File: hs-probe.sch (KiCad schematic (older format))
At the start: 55 parts, among them J1 USB_C_Receptacle_USB2.0, J2 Castellated Vias, J3 Castellated Vias, J4 Castellated Vias, J5 tag-connect-swd, U1 base-stm32, U2 12 MHz, U3 MIC5353, U4 NUF8401MNT4G, U5 STDC14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

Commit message: Revert accidential commits that should have gone to a fork
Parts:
- U1: value base-stm32 -> hs-probe-stm32; symbol base-stm32:base-stm32 -> hs-probe-stm32:hs-probe-stm32
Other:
- note added: "Designed by: Emil Fresk\nTwitter / Github: @korken89\nLink: https://github.com/probe-rs/hs-probe"
- note removed: "Designed by: Emil Fresk\nTwitter / Github: @korken89\nLink: https://github.com/probe-rs/base"
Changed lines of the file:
@@
 MCU I/O
 $Comp
-L base-stm32:base-stm32 U1
+L hs-probe-stm32:hs-probe-stm32 U1
 U 9 1 5F18CA2E
 P 5550 5500
 F 0 "U1" H 6042 5787 60  0000 C CNN
-F 1 "base-stm32" H 6042 5681 60  0000 C CNN
+F 1 "hs-probe-stm32" H 6042 5681 60  0000 C CNN
 F 2 "bga:UFBGA-201_10x10mm_Layout15x15_P0.65mm" H 5750 5550 60  0001 L CNN
 F 3 "" H 5750 5350 60  0001 L CNN
@@
 $EndComp
 $Comp
-L base-stm32:base-stm32 U1
+L hs-probe-stm32:hs-probe-stm32 U1
 U 7 1 5F17D932
 P 3900 9500
 F 0 "U1" H 4342 9787 60  0000 C CNN
-F 1 "base-stm32" H 4342 9681 60  0000 C CNN
+F 1 "hs-probe-stm32" H 4342 9681 60  0000 C CNN
 F 2 "bga:UFBGA-201_10x10mm_Layout15x15_P0.65mm" H 4100 9550 60  0001 L CNN
 F 3 "" H 4100 9350 60  0001 L CNN
@@
 $EndComp
 $Comp
-L base-stm32:base-stm32 U1
+L hs-probe-stm32:hs-probe-stm32 U1
 U 5 1 5F175F3E
 P 3900 7500
 F 0 "U1" H 4342 7787 60  0000 C CNN
-F 1 "base-stm32" H 4342 7681 60  0000 C CNN
+F 1 "hs-probe-stm32" H 4342 7681 60  0000 C CNN
 F 2 "bga:UFBGA-201_10x10mm_Layout15x15_P0.65mm" H 4100 7550 60  0001 L CNN
 F 3 "" H 4100 7350 60  0001 L CNN
@@
 $EndComp
 $Comp
-L base-stm32:base-stm32 U1
+L hs-probe-stm32:hs-probe-stm32 U1
 U 4 1 5F17144F
 P 3900 5500
 F 0 "U1" H 4392 5787 60  0000 C CNN
-F 1 "base-stm32" H 4392 5681 60  0000 C CNN
+F 1 "hs-probe-stm32" H 4392 5681 60  0000 C CNN
 F 2 "bga:UFBGA-201_10x10mm_Layout15x15_P0.65mm" H 4100 5550 60  0001 L CNN
 F 3 "" H 4100 5350 60  0001 L CNN
@@
 $EndComp
 $Comp
-L base-stm32:base-stm32 U1
+L hs-probe-stm32:hs-probe-stm32 U1
 U 3 1 5F16E354
 P 2150 9300
 F 0 "U1" H 2642 9587 60  0000 C CNN
-F 1 "base-stm32" H 2642 9481 60  0000 C CNN
+F 1 "hs-probe-stm32" H 2642 9481 60  0000 C CNN
 F 2 "bga:UFBGA-201_10x10mm_Layout15x15_P0.65mm" H 2350 9350 60  0001 L CNN
 F 3 "" H 2350 9150 60  0001 L CNN
@@
 $EndComp
 $Comp
-L base-stm32:base-stm32 U1
+L hs-probe-stm32:hs-probe-stm32 U1
 U 2 1 5F165849
 P 2150 7300
 F 0 "U1" H 2792 7587 60  0000 C CNN
-F 1 "base-stm32" H 2792 7481 60  0000 C CNN
+F 1 "hs-probe-stm32" H 2792 7481 60  0000 C CNN
 F 2 "bga:UFBGA-201_10x10mm_Layout15x15_P0.65mm" H 2350 7350 60  0001 L CNN
 F 3 "" H 2350 7150 60  0001 L CNN
@@
 $EndComp
 $Comp
-L base-stm32:base-stm32 U1
+L hs-probe-stm32:hs-probe-stm32 U1
 U 1 1 5F160B70
 P 2150 5500
 F 0 "U1" H 2792 5787 60  0000 C CNN
-F 1 "base-stm32" H 2792 5681 60  0000 C CNN
+F 1 "hs-probe-stm32" H 2792 5681 60  0000 C CNN
 F 2 "bga:UFBGA-201_10x10mm_Layout15x15_P0.65mm" H 2350 5550 60  0001 L CNN
 F 3 "" H 2350 5350 60  0001 L CNN
@@
 $EndComp
 $Comp
-L base-stm32:base-stm32 U1
+L hs-probe-stm32:hs-probe-stm32 U1
 U 12 1 5F19B372
 P 1550 2000
 F 0 "U1" H 1892 2287 60  0000 C CNN
-F 1 "base-stm32" H 1892 2181 60  0000 C CNN
+F 1 "hs-probe-stm32" H 1892 2181 60  0000 C CNN
 F 2 "bga:UFBGA-201_10x10mm_Layout15x15_P0.65mm" H 1750 2050 60  0001 L CNN
 F 3 "" H 1750 1850 60  0001 L CNN
@@
 $EndComp
 $Comp
-L base-stm32:base-stm32 U1
+L hs-probe-stm32:hs-probe-stm32 U1
 U 11 1 5F19563C
 P 4100 2000
 F 0 "U1" H 4517 2287 60  0000 C CNN
-F 1 "base-stm32" H 4517 2181 60  0000 C CNN
+F 1 "hs-probe-stm32" H 4517 2181 60  0000 C CNN
 F 2 "bga:UFBGA-201_10x10mm_Layout15x15_P0.65mm" H 4300 2050 60  0001 L CNN
 F 3 "" H 4300 1850 60  0001 L CNN
@@
 $EndComp
 $Comp
-L base-stm32:base-stm32 U1
+L hs-probe-stm32:hs-probe-stm32 U1
 U 10 1 5F190F67
 P 2350 3650
 F 0 "U1" H 3092 3937 60  0000 C CNN
-F 1 "base-stm32" H 3092 3831 60  0000 C CNN
+F 1 "hs-probe-stm32" H 3092 3831 60  0000 C CNN
 F 2 "bga:UFBGA-201_10x10mm_Layout15x15_P0.65mm" H 2550 3700 60  0001 L CNN
 F 3 "" H 2550 3500 60  0001 L CNN
@@
 SPI1_MOSI
 Text Notes 11900 10500 0    100  ~ 0
-Designed by: Emil Fresk\nTwitter / Github: @korken89\nLink: https://github.com/probe-rs/base
+Designed by: Emil Fresk\nTwitter / Github: @korken89\nLink: https://github.com/probe-rs/hs-probe
 NoConn ~ 2150 5500
 NoConn ~ 2150 5600

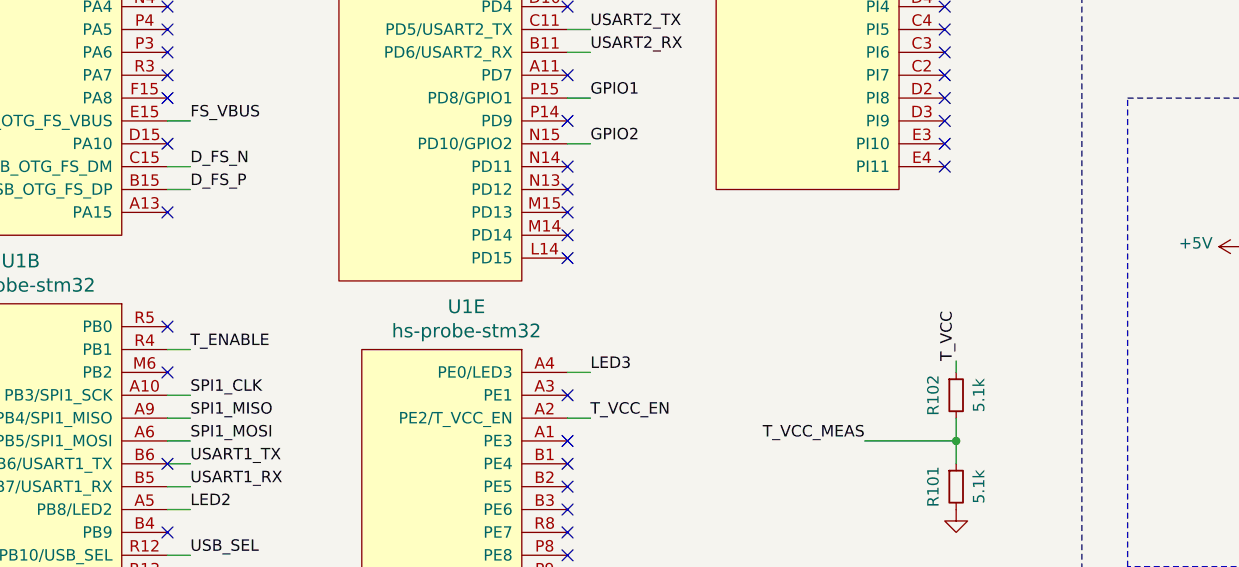
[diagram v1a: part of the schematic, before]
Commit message: Added 5V target sense line
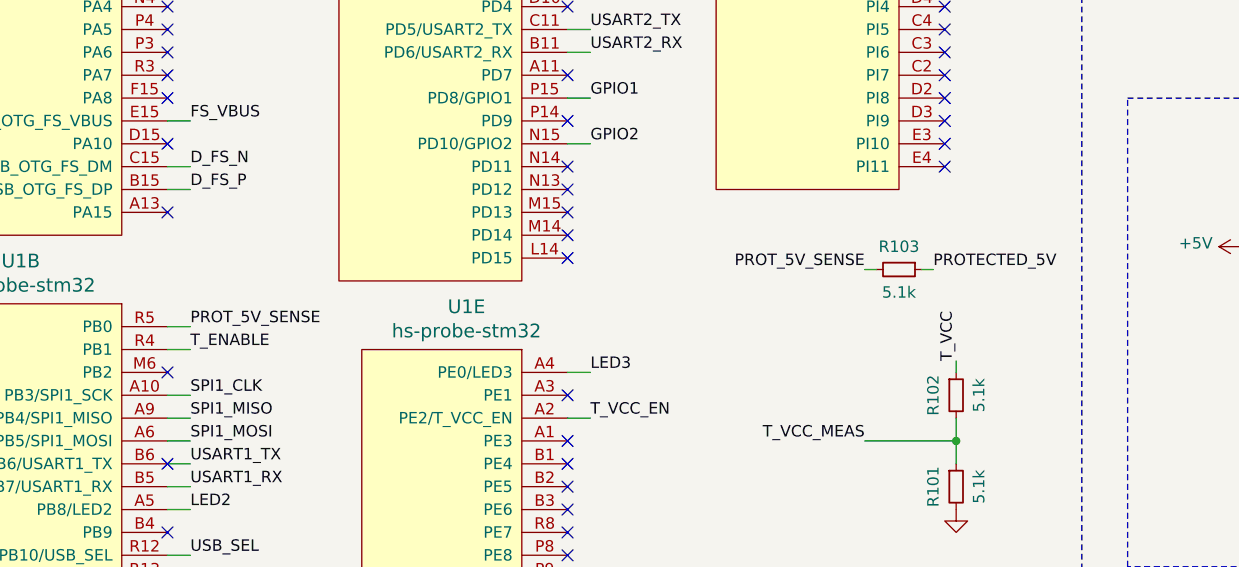
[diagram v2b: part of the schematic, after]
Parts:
- added R103: 5.1k, passive:R_0402, symbol Device:R_Small
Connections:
- net PROTECTED_5V: now also R103.1
- net PROT_5V_SENSE: now reaches U1.R5 (PB0)
- net PROT_5V_SENSE: now also R103.2
- no-connect marks 86 -> 85
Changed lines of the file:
@@
 NoConn ~ 2150 6500
 NoConn ~ 2150 6800
-NoConn ~ 2150 7300
 NoConn ~ 2150 7500
 NoConn ~ 2150 8200
@@
 Wire Wire Line
 	7450 7900 7550 7900
+$Comp
+L Device:R_Small R103
+U 1 1 5FB7207F
+P 5350 7050
+F 0 "R103" V 5250 7050 50  0000 C CNN
+F 1 "5.1k" V 5450 7050 50  0000 C CNN
+F 2 "passive:R_0402" H 5350 7050 50  0001 C CNN
+F 3 "~" H 5350 7050 50  0001 C CNN
+F 4 "1%" H 5350 7050 50  0001 C CNN "Tolerance"
+	1    5350 7050
+	0    1    1    0
+$EndComp
+Text Label 5500 7050 0    50   ~ 0
+PROTECTED_5V
+Wire Wire Line
+	5500 7050 5450 7050
+Wire Wire Line
+	5250 7050 5200 7050
+Text Label 5200 7050 2    50   ~ 0
+PROT_5V_SENSE
+Text Label 2250 7300 0    50   ~ 0
+PROT_5V_SENSE
+Wire Wire Line
+	2150 7300 2250 7300
 $EndSCHEMATC

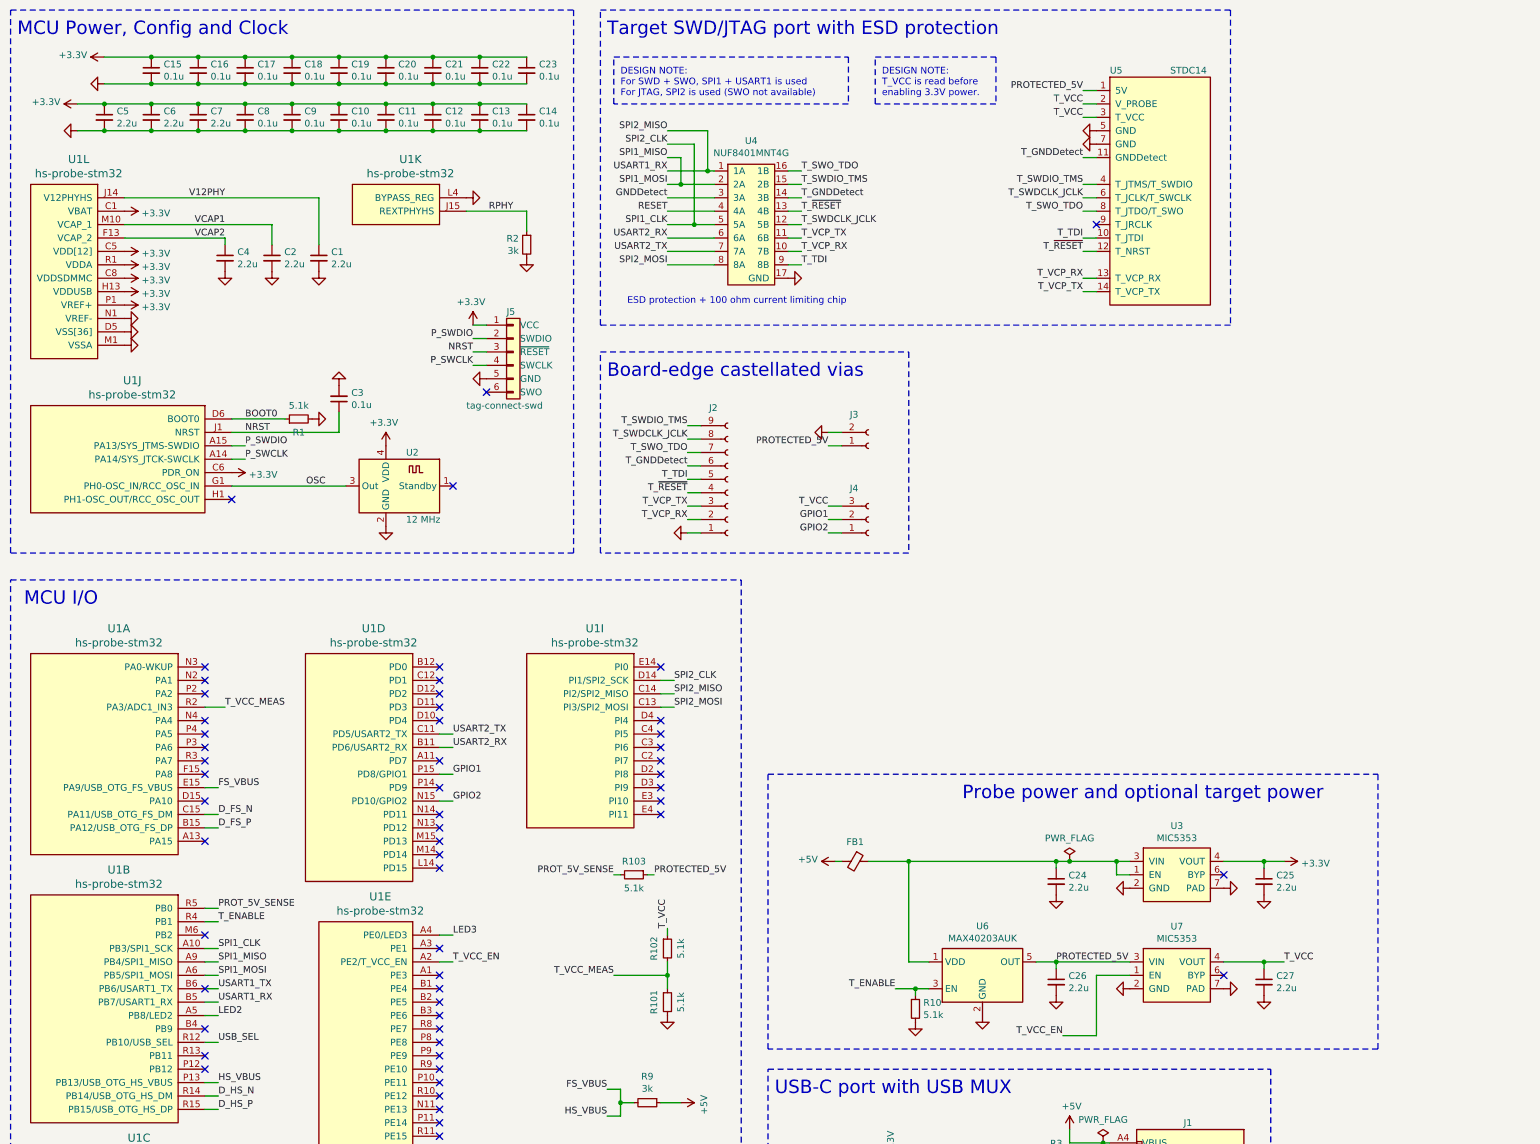
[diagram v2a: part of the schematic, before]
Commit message: v1.3, now can connect 5V to pin 7 of STDC14
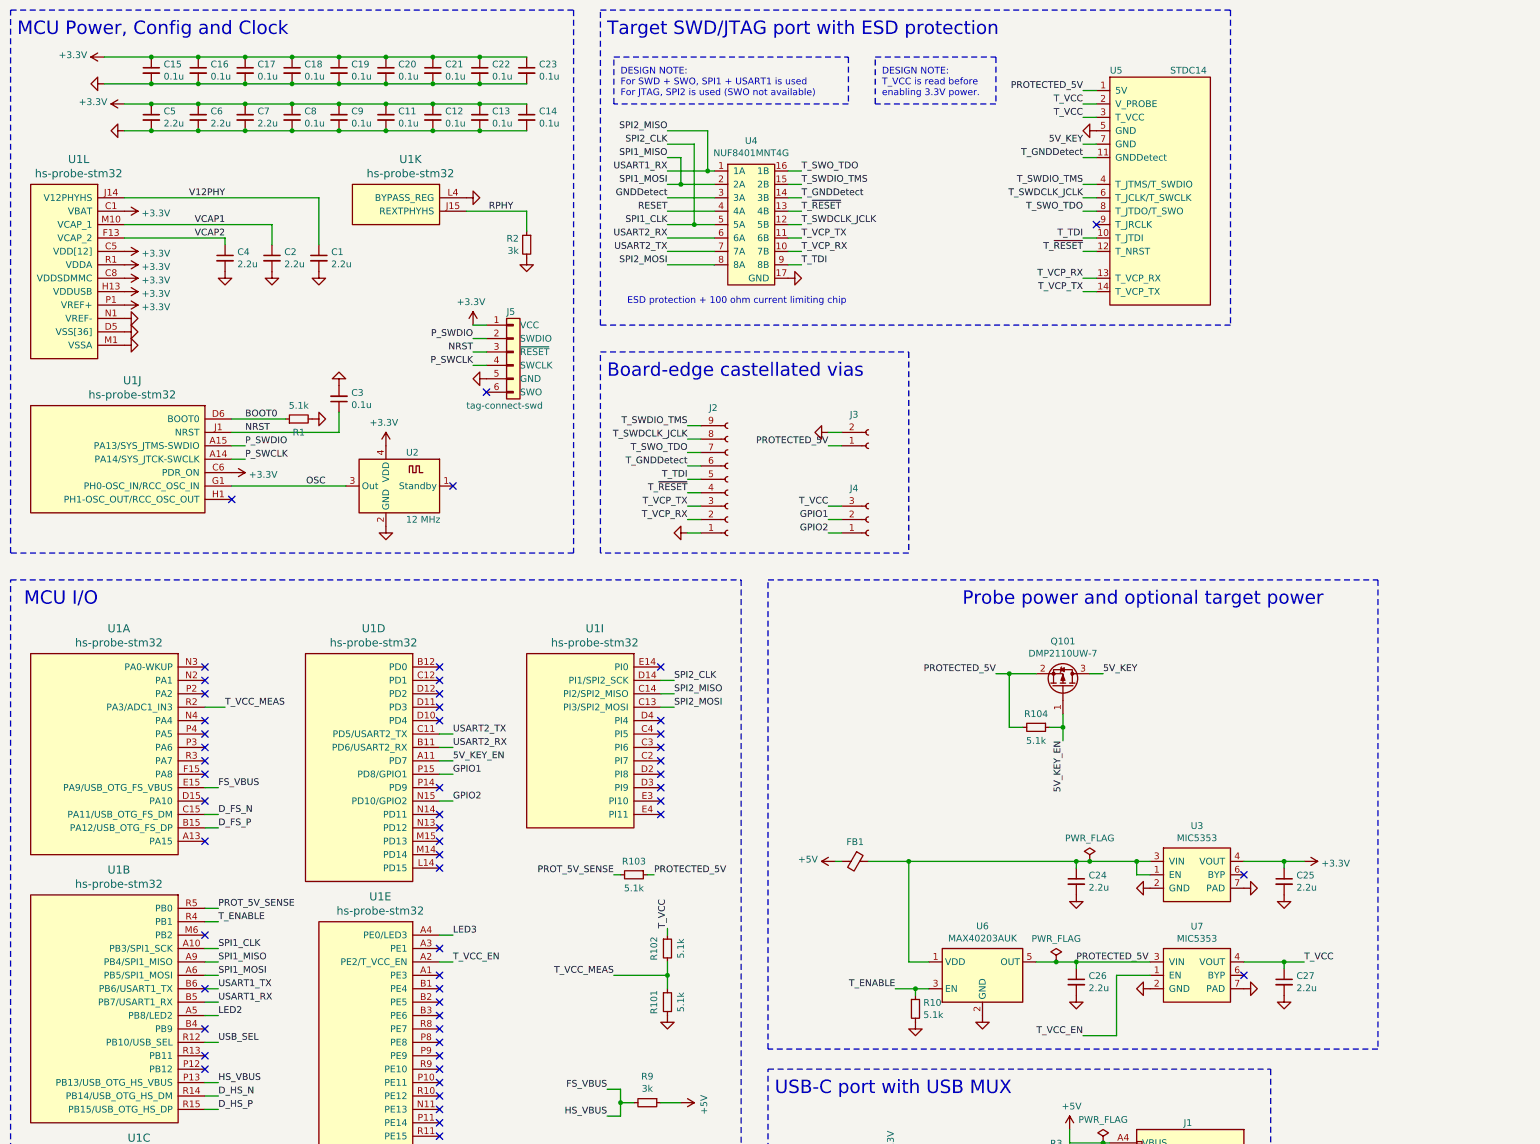
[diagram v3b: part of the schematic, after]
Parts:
- removed C10: 0.1u, passive:C_0402, symbol Device:C_Small
- added Q101: DMP2110UW-7, sot:SOT-323, symbol Device:Q_PMOS_GSD
- added R104: 5.1k, passive:R_0402, symbol Device:R_Small
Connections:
- net GND: no longer U5.7 (GND)
- net PROTECTED_5V: now also Q101.2 (S), R104.2
- net 5V_KEY_EN: now reaches U1.A11 (PD7)
- net 5V_KEY_EN: now also Q101.1 (G), R104.1
- new net 5V_KEY: Q101.3 (D), U5.7 (GND)
- no-connect marks 85 -> 84
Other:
- moved on the sheet: C24, C25, C26, C27, C5, C6, C7, C8, C9, U3, U7

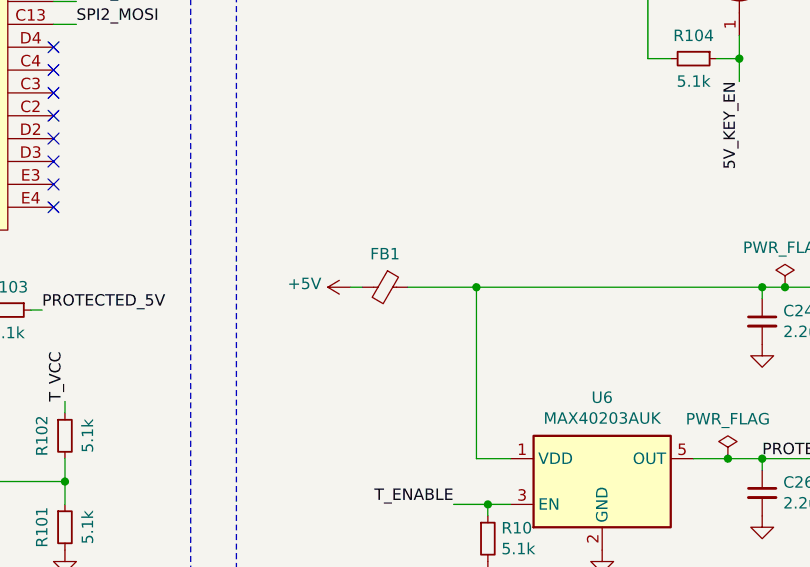
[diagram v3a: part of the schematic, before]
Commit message: Changed ferrite bead for fuse
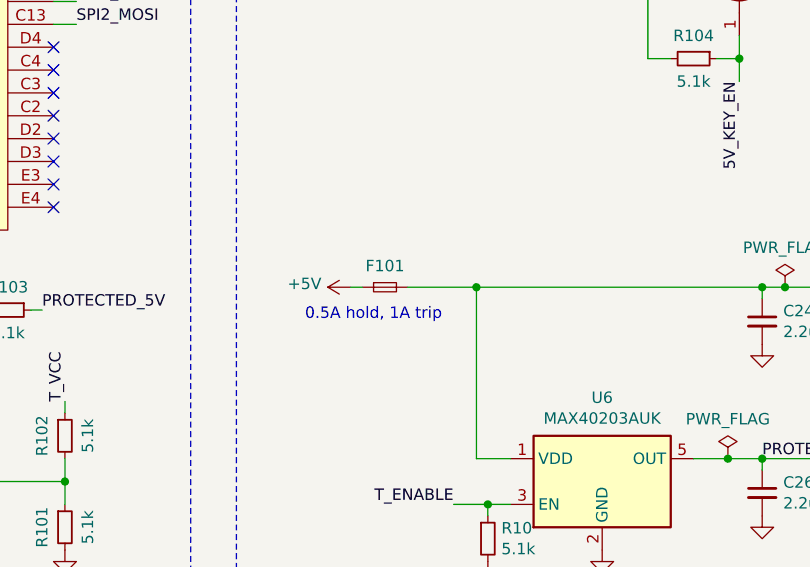
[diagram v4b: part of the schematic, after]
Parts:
- removed FB1: Ferrite_Bead_Small, passive:R_0402, symbol Device:Ferrite_Bead_Small
- added F101: Fuse_Small, Fuse:Fuse_0603_1608Metric, symbol Device:Fuse_Small
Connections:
- net +5V: now also F101.1
- net at C24.1, U3.1 (EN), U3.3 (VIN)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: now also F101.2
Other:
- note added: "0.5A hold, 1A trip"
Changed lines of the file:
@@
 	0    -1   -1   0
-$EndComp
-$Comp
-L Device:Ferrite_Bead_Small FB1
-U 1 1 5EA8C637
-P 7000 6950
-F 0 "FB1" V 6855 6950 50  0000 C CNN
-F 1 "Ferrite_Bead_Small" V 6854 6950 50  0001 C CNN
-F 2 "passive:R_0402" V 6930 6950 50  0001 C CNN
-F 3 "~" H 7000 6950 50  0001 C CNN
-F 4 "MMZ1005S601HT000" H 7000 6950 50  0001 C CNN "MPN"
-F 5 "600 Ohm @ 100 MHz" H 7000 6950 50  0001 C CNN "Tolerance"
-	1    7000 6950
-	0    1    1    0
 $EndComp
 Wire Wire Line
@@
 	8700 1600 8800 1600
 $Comp
-L power:PWR_FLAG #FLG?
+L power:PWR_FLAG #FLG0104
 U 1 1 5FF2DABB
 P 8500 7700
-F 0 "#FLG?" H 8500 7775 50  0001 C CNN
+F 0 "#FLG0104" H 8500 7775 50  0001 C CNN
 F 1 "PWR_FLAG" H 8500 7873 50  0000 C CNN
 F 2 "" H 8500 7700 50  0001 C CNN
@@
 Wire Wire Line
 	8500 7700 8650 7700
+$Comp
+L Device:Fuse_Small F101
+U 1 1 5FC42F3E
+P 7000 6950
+F 0 "F101" H 7000 7043 50  0000 C CNN
+F 1 "Fuse_Small" H 7000 7044 50  0001 C CNN
+F 2 "Fuse:Fuse_0603_1608Metric" H 7000 6950 50  0001 C CNN
+F 3 "https://www.bourns.com/docs/Product-Datasheets/mffsmf.pdf" H 7000 6950 50  0001 C CNN
+F 4 " MF-FSMF050X-2" H 7000 6950 50  0001 C CNN "MFPN"
+	1    7000 6950
+	1    0    0    -1
+$EndComp
+Text Notes 6650 7100 0    50   ~ 0
+0.5A hold, 1A trip
 $EndSCHEMATC
